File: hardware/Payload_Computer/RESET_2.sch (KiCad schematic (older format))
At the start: 1 part

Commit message: More Library Updates
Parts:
- S?: symbol Payload_Computer-rescue:GPTS203211B-Symbols -> Symbols:GPTS203211B
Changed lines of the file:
@@
 $EndDescr
 $Comp
-L Payload_Computer-rescue:GPTS203211B-Symbols S?
+L Symbols:GPTS203211B S?
 U 1 1 5F8EEC81
 P 5800 3850

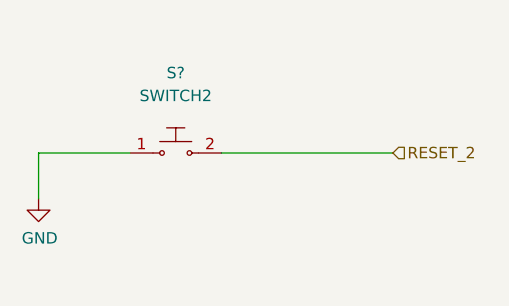
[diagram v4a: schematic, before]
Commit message: Finished Fan Schematic. Working on Servos
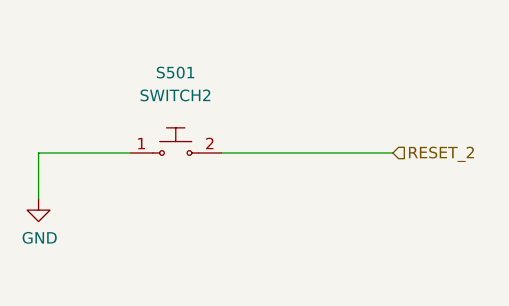
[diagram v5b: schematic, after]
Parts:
- gave numbers to parts that had none: 1
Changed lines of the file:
@@
 $Descr A4 11693 8268
 encoding utf-8
-Sheet 5 26
+Sheet 5 22
 Title ""
 Date ""
@@
 P 5800 3850
 AR Path="/5F8EA469/5F8EEC81" Ref="S?"  Part="1"
-AR Path="/5F8EA4F9/5F8EEC81" Ref="S?"  Part="1"
-F 0 "S?" H 5800 4200 50  0000 C CNN
+AR Path="/5F8EA4F9/5F8EEC81" Ref="S501"  Part="1"
+F 0 "S501" H 5800 4200 50  0000 C CNN
 F 1 "SWITCH2" H 5800 4100 50  0000 C CNN
 F 2 "" H 6000 4050 50  0001 L CNN
